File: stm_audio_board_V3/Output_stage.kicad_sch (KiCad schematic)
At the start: 29 parts, among them U2 OP275

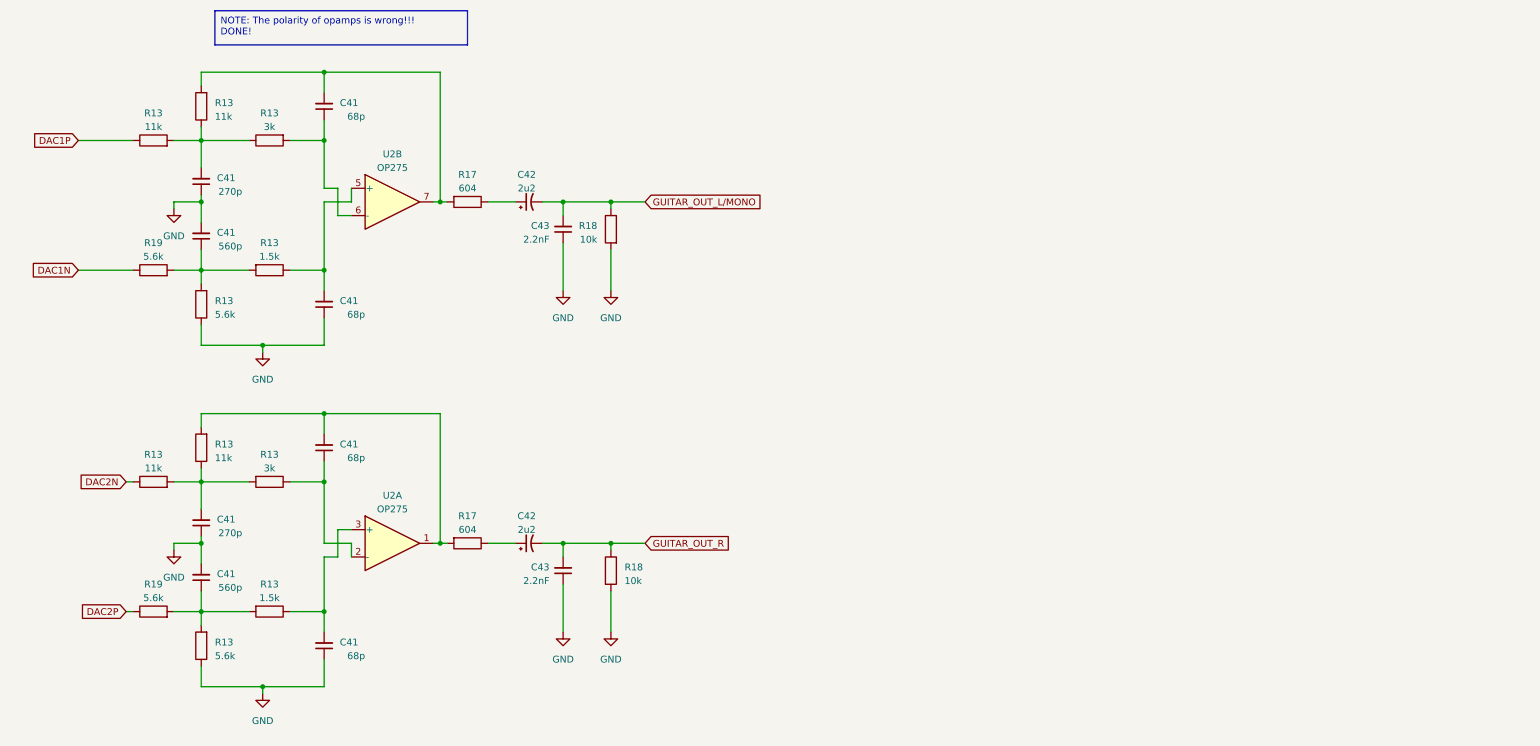
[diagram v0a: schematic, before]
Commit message: Input and output stages are made and assembly started on pcb view
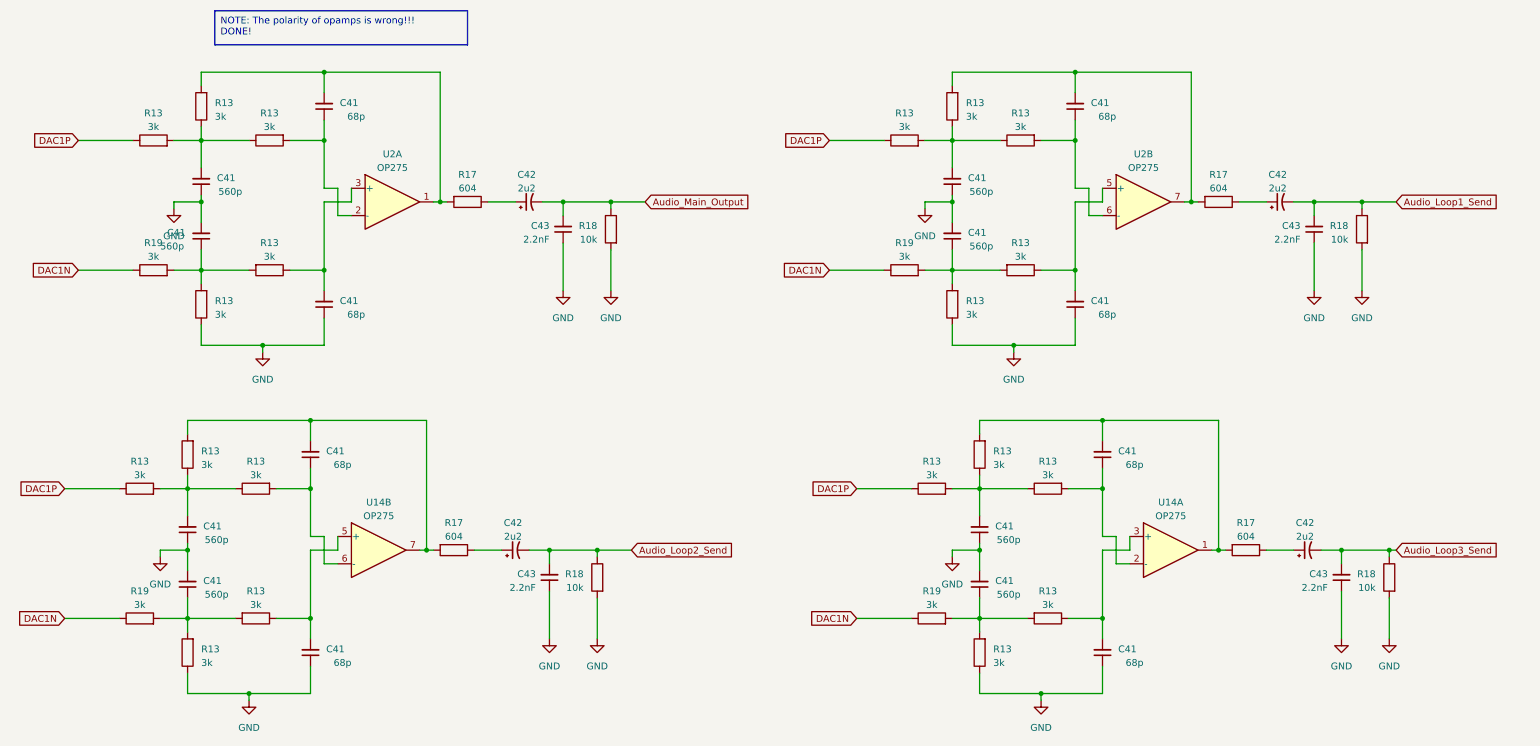
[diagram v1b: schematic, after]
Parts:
- removed C41: 560p, Capacitor_SMD:C_0603_1608Metric_Pad1.08x0.95mm_HandSolder, symbol Device:C_Small
- removed C41 (x2): 68p, Capacitor_SMD:C_0603_1608Metric_Pad1.08x0.95mm_HandSolder, symbol Device:C_Small
- removed C41: 270p, Capacitor_SMD:C_0603_1608Metric_Pad1.08x0.95mm_HandSolder, symbol Device:C_Small
- removed C42: 2u2, Capacitor_SMD:C_0805_2012Metric_Pad1.18x1.45mm_HandSolder, symbol Device:C_Polarized_Small_US
- removed C43: 2.2nF, Capacitor_SMD:C_0603_1608Metric_Pad1.08x0.95mm_HandSolder, symbol Device:C_Small
- removed R13: 3k, Resistor_SMD:R_0805_2012Metric_Pad1.20x1.40mm_HandSolder, symbol Device:R
- removed R13, R19: 5.6k, Resistor_SMD:R_0805_2012Metric_Pad1.20x1.40mm_HandSolder, symbol Device:R
- removed R13 (x2): 11k, Resistor_SMD:R_0805_2012Metric_Pad1.20x1.40mm_HandSolder, symbol Device:R
- removed R13: 1.5k, Resistor_SMD:R_0805_2012Metric_Pad1.20x1.40mm_HandSolder, symbol Device:R
- removed R17: 604, Resistor_SMD:R_0805_2012Metric_Pad1.20x1.40mm_HandSolder, symbol Device:R
- removed R18: 10k, Resistor_SMD:R_0805_2012Metric_Pad1.20x1.40mm_HandSolder, symbol Device:R
- removed unit 1 of U2
- added C41 (x6): 560p, Capacitor_SMD:C_0603_1608Metric, symbol Device:C_Small
- added C41 (x6): 68p, Capacitor_SMD:C_0603_1608Metric, symbol Device:C_Small
- added C42 (x3): 2u2, Capacitor_SMD:C_0805_2012Metric_Pad1.18x1.45mm_HandSolder, symbol Device:C_Polarized_Small_US
- added C43 (x3): 2.2nF, Capacitor_SMD:C_0603_1608Metric, symbol Device:C_Small
- added R13 (x15), R19 (x3): 3k, Resistor_SMD:R_0603_1608Metric, symbol Device:R
- added R17 (x3): 604, Resistor_SMD:R_0603_1608Metric, symbol Device:R
- added R18 (x3): 10k, Resistor_SMD:R_0603_1608Metric, symbol Device:R
- added U14: OP275, Package_SO:SSOP-8_3.9x5.05mm_P1.27mm, symbol Amplifier_Operational:OP275
- added unit 2 of U2
- C41, C43: footprint Capacitor_SMD:C_0603_1608Metric_Pad1.08x0.95mm_HandSolder -> Capacitor_SMD:C_0603_1608Metric
- C41: value 270p -> 560p; footprint Capacitor_SMD:C_0603_1608Metric_Pad1.08x0.95mm_HandSolder -> Capacitor_SMD:C_0603_1608Metric
- R13, R17, R18: footprint Resistor_SMD:R_0805_2012Metric_Pad1.20x1.40mm_HandSolder -> Resistor_SMD:R_0603_1608Metric
- R13: value 11k -> 3k; footprint Resistor_SMD:R_0805_2012Metric_Pad1.20x1.40mm_HandSolder -> Resistor_SMD:R_0603_1608Metric
- R13: value 1.5k -> 3k; footprint Resistor_SMD:R_0805_2012Metric_Pad1.20x1.40mm_HandSolder -> Resistor_SMD:R_0603_1608Metric
- R13, R19: value 5.6k -> 3k; footprint Resistor_SMD:R_0805_2012Metric_Pad1.20x1.40mm_HandSolder -> Resistor_SMD:R_0603_1608Metric
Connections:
- net DAC1N: now also R19.1, R19.1, R19.1
- net DAC1P: now also R13.1, R13.1, R13.1
- net GND: now also C41.1, C41.1, C41.1, C41.1, C41.1, C41.1, C41.2, C41.2, C41.2, C43.1, C43.1, C43.1, R13.1, R13.1, R13.1, R18.2, R18.2, R18.2
- net at C41.2, R13.2, R17.2: now also U2.1; no longer U2.7
- net at C41.1, R13.2: now also U2.2 (-); no longer U2.6 (-)
- net at C41.2, R13.1: now also U2.3 (+); no longer U2.5 (+)
- net GUITAR_OUT_L/MONO renamed Audio_Main_Output
- new net: C42.1, R17.1 (x3)
- new net: C41.2, R13.1, U14.5 (+)
- new net: C41.1, R13.2, U14.6 (-)
- new net: C41.2, R13.2, R17.2, U14.7
- new net: C41.2, R13.1, R13.1, R13.2 (x3)
- new net: C41.2, R13.2, R17.2, U14.1
- new net: C41.2, R13.1, U2.5 (+)
- new net: C41.1, R13.2, U2.6 (-)
- new net: C41.2, R13.2, R17.2, U2.7
- new net: C41.1, R13.2, R13.2, R19.2 (x3)
- new net: C41.1, R13.2, U14.2 (-)
- new net: C41.2, R13.1, U14.3 (+)
- new net Audio_Loop1_Send: C42.2, C43.2, R18.1
- new net Audio_Loop2_Send: C42.2, C43.2, R18.1
- new net Audio_Loop3_Send: C42.2, C43.2, R18.1
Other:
- moved on the sheet: C41

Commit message: Input output connected to codec
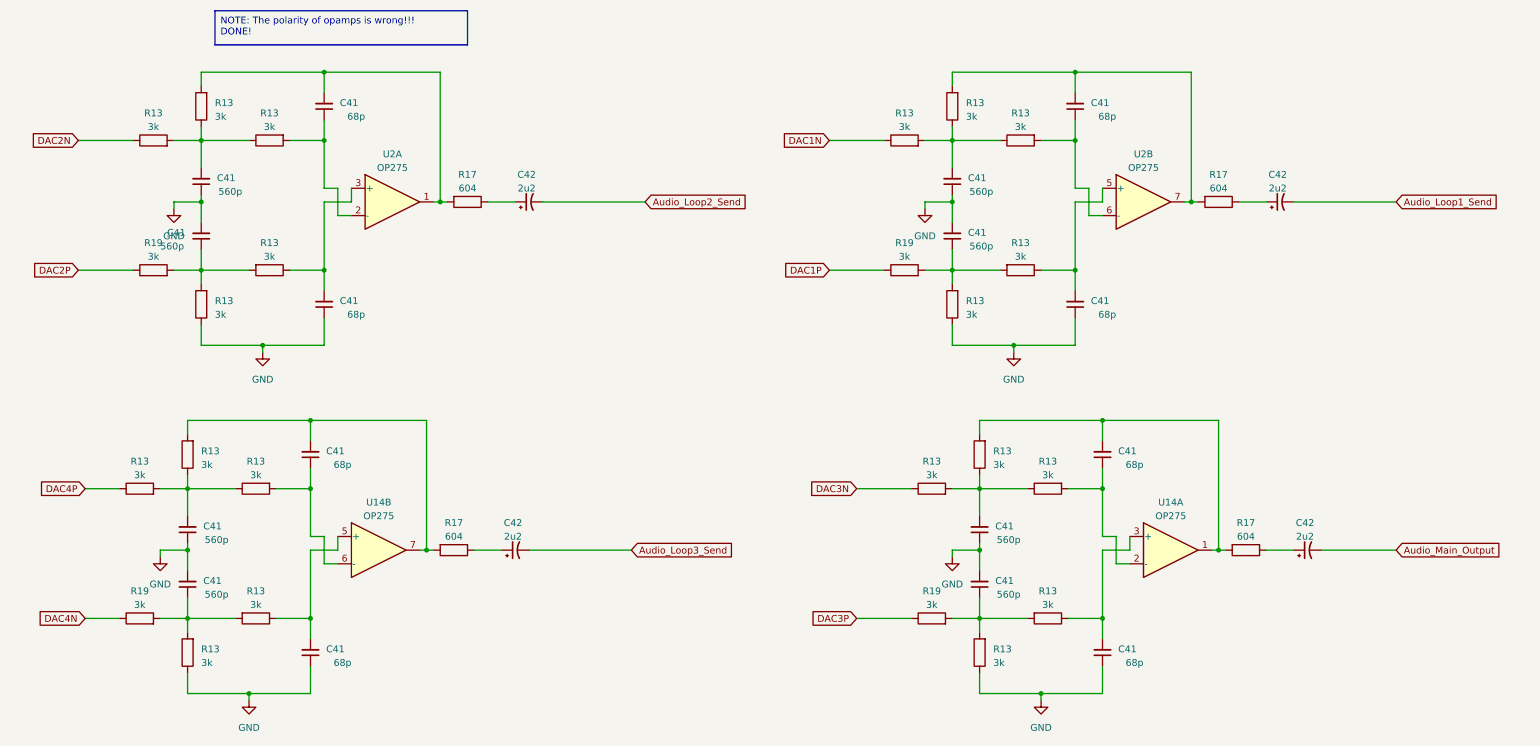
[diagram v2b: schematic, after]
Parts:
- removed C43 (x4): 2.2nF, Capacitor_SMD:C_0603_1608Metric, symbol Device:C_Small
- removed R18 (x4): 10k, Resistor_SMD:R_0603_1608Metric, symbol Device:R
- U14, U2: JLCPCB (none) -> C161797
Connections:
- net Audio_Loop2_Send: now also C42.2; no longer C42.2
- net Audio_Loop3_Send: now also C42.2; no longer C42.2
- net Audio_Main_Output: now also C42.2; no longer C42.2
- net DAC1N: now also R13.1; no longer R19.1, R19.1, R19.1, R19.1
- net DAC1P: now also R19.1; no longer R13.1, R13.1, R13.1, R13.1
- new net DAC2N: R13.1
- new net DAC2P: R19.1
- new net DAC3N: R13.1
- new net DAC3P: R19.1
- new net DAC4N: R19.1
- new net DAC4P: R13.1

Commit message: Reworked outline for enclosure
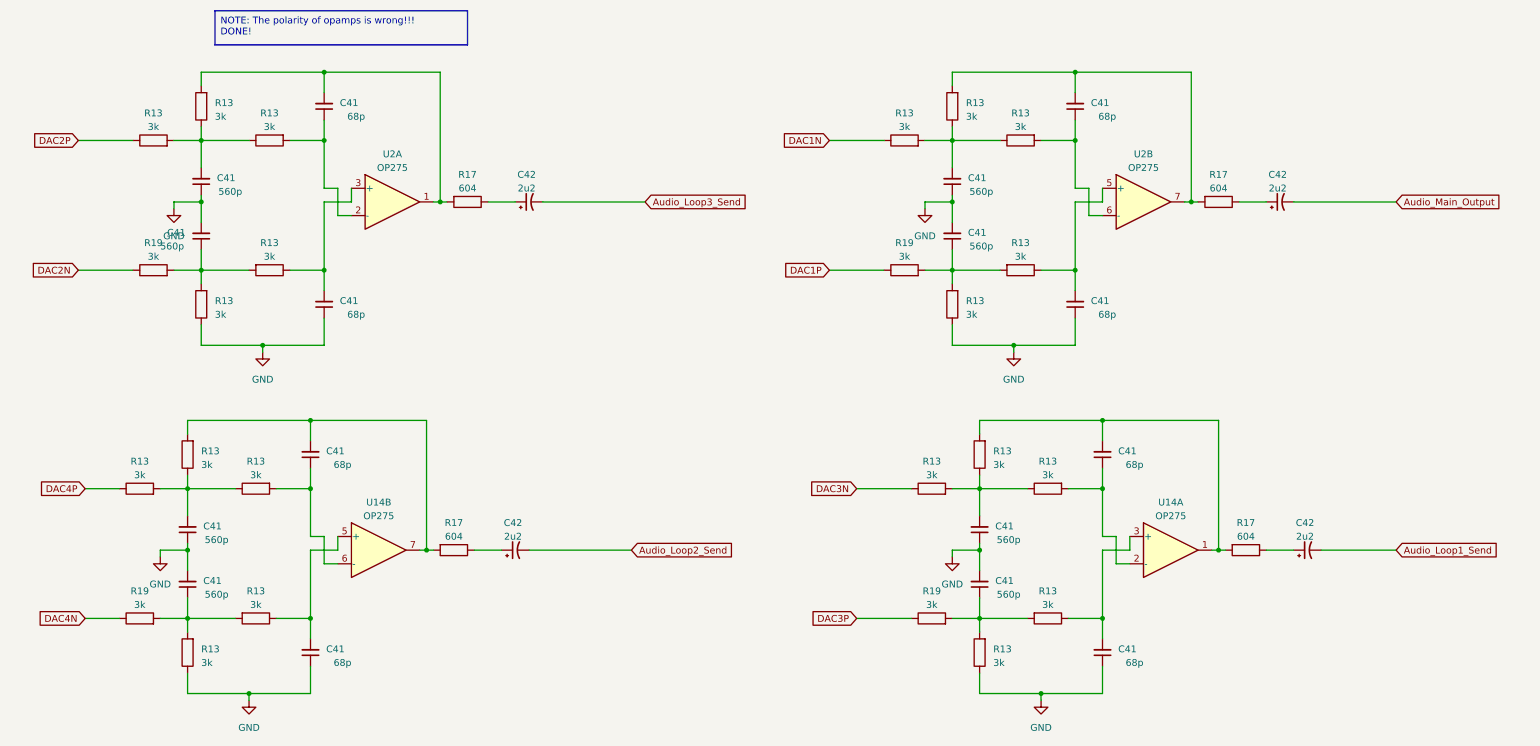
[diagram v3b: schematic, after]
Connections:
- net Audio_Loop1_Send: now also C42.2; no longer C42.2
- net Audio_Loop2_Send: now also C42.2; no longer C42.2
- net Audio_Loop3_Send: now also C42.2; no longer C42.2
- net Audio_Main_Output: now also C42.2; no longer C42.2
- net DAC2N: now also R19.1; no longer R13.1
- net DAC2P: now also R13.1; no longer R19.1
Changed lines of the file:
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@@
     (effects (font (size 1.27 1.27)) (justify left top))
+  )
+  (global_label "DAC2N" (shape input) (at 69.85 82.55 180) (fields_autoplaced)
+    (effects (font (size 1.27 1.27)) (justify right))
+    (property "Intersheetrefs" "${INTERSHEET_REFS}" (at 60.7756 82.55 0)
+      (effects (font (size 1.27 1.27)) (justify right) hide)
+    )
+  )
+  (global_label "Audio_Loop1_Send" (shape input) (at 314.96 134.62 0) (fields_autoplaced)
+    (effects (font (size 1.27 1.27)) (justify left))
+    (property "Intersheetrefs" "${INTERSHEET_REFS}" (at 335.2221 134.62 0)
+      (effects (font (size 1.27 1.27)) (justify left) hide)
+    )
   )
   (global_label "DAC4P" (shape input) (at 71.12 123.19 180) (fields_autoplaced)
@@
     )
   )
-  (global_label "DAC2P" (shape input) (at 69.85 82.55 180) (fields_autoplaced)
-    (effects (font (size 1.27 1.27)) (justify right))
-    (property "Intersheetrefs" "${INTERSHEET_REFS}" (at 60.8361 82.55 0)
-      (effects (font (size 1.27 1.27)) (justify right) hide)
-    )
-  )
-  (global_label "DAC2N" (shape input) (at 69.85 58.42 180) (fields_autoplaced)
-    (effects (font (size 1.27 1.27)) (justify right))
-    (property "Intersheetrefs" "${INTERSHEET_REFS}" (at 60.7756 58.42 0)
-      (effects (font (size 1.27 1.27)) (justify right) hide)
+  (global_label "Audio_Main_Output" (shape input) (at 314.96 69.85 0) (fields_autoplaced)
+    (effects (font (size 1.27 1.27)) (justify left))
+    (property "Intersheetrefs" "${INTERSHEET_REFS}" (at 335.5245 69.85 0)
+      (effects (font (size 1.27 1.27)) (justify left) hide)
     )
   )
@@
     (property "Intersheetrefs" "${INTERSHEET_REFS}" (at 200.5361 82.55 0)
       (effects (font (size 1.27 1.27)) (justify right) hide)
-    )
-  )
-  (global_label "Audio_Main_Output" (shape input) (at 314.96 134.62 0) (fields_autoplaced)
-    (effects (font (size 1.27 1.27)) (justify left))
-    (property "Intersheetrefs" "${INTERSHEET_REFS}" (at 335.5245 134.62 0)
-      (effects (font (size 1.27 1.27)) (justify left) hide)
-    )
-  )
-  (global_label "Audio_Loop1_Send" (shape input) (at 314.96 69.85 0) (fields_autoplaced)
-    (effects (font (size 1.27 1.27)) (justify left))
-    (property "Intersheetrefs" "${INTERSHEET_REFS}" (at 335.2221 69.85 0)
-      (effects (font (size 1.27 1.27)) (justify left) hide)
     )
   )
@@
     )
   )
-  (global_label "Audio_Loop3_Send" (shape input) (at 172.72 134.62 0) (fields_autoplaced)
+  (global_label "Audio_Loop2_Send" (shape input) (at 172.72 134.62 0) (fields_autoplaced)
     (effects (font (size 1.27 1.27)) (justify left))
     (property "Intersheetrefs" "${INTERSHEET_REFS}" (at 192.9821 134.62 0)
       (effects (font (size 1.27 1.27)) (justify left) hide)
+    )
+  )
+  (global_label "DAC2P" (shape input) (at 69.85 58.42 180) (fields_autoplaced)
+    (effects (font (size 1.27 1.27)) (justify right))
+    (property "Intersheetrefs" "${INTERSHEET_REFS}" (at 60.8361 58.42 0)
+      (effects (font (size 1.27 1.27)) (justify right) hide)
     )
   )
@@
     )
   )
-  (global_label "Audio_Loop2_Send" (shape input) (at 175.26 69.85 0) (fields_autoplaced)
+  (global_label "Audio_Loop3_Send" (shape input) (at 175.26 69.85 0) (fields_autoplaced)
     (effects (font (size 1.27 1.27)) (justify left))
     (property "Intersheetrefs" "${INTERSHEET_REFS}" (at 195.5221 69.85 0)
